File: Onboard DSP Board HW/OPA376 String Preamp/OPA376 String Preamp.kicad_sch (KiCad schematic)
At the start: 8 parts, among them U5 OPA376AIDCKT

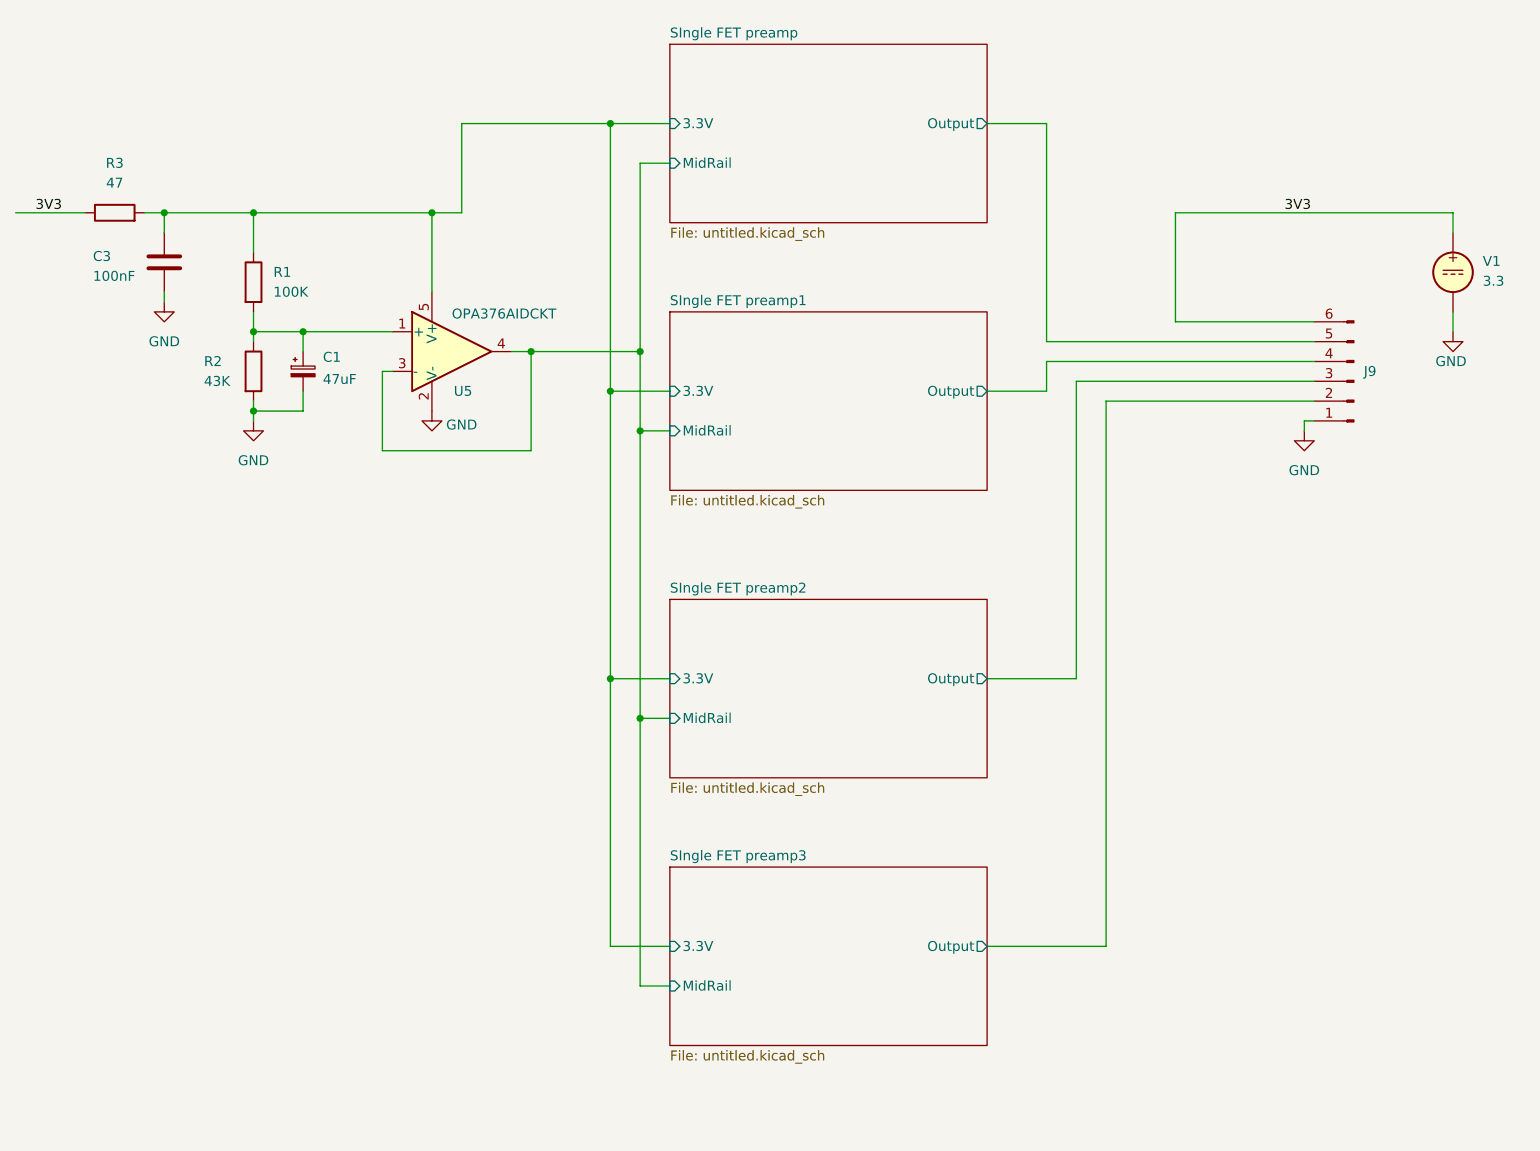
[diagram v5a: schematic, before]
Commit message: preamp board modified and simulated
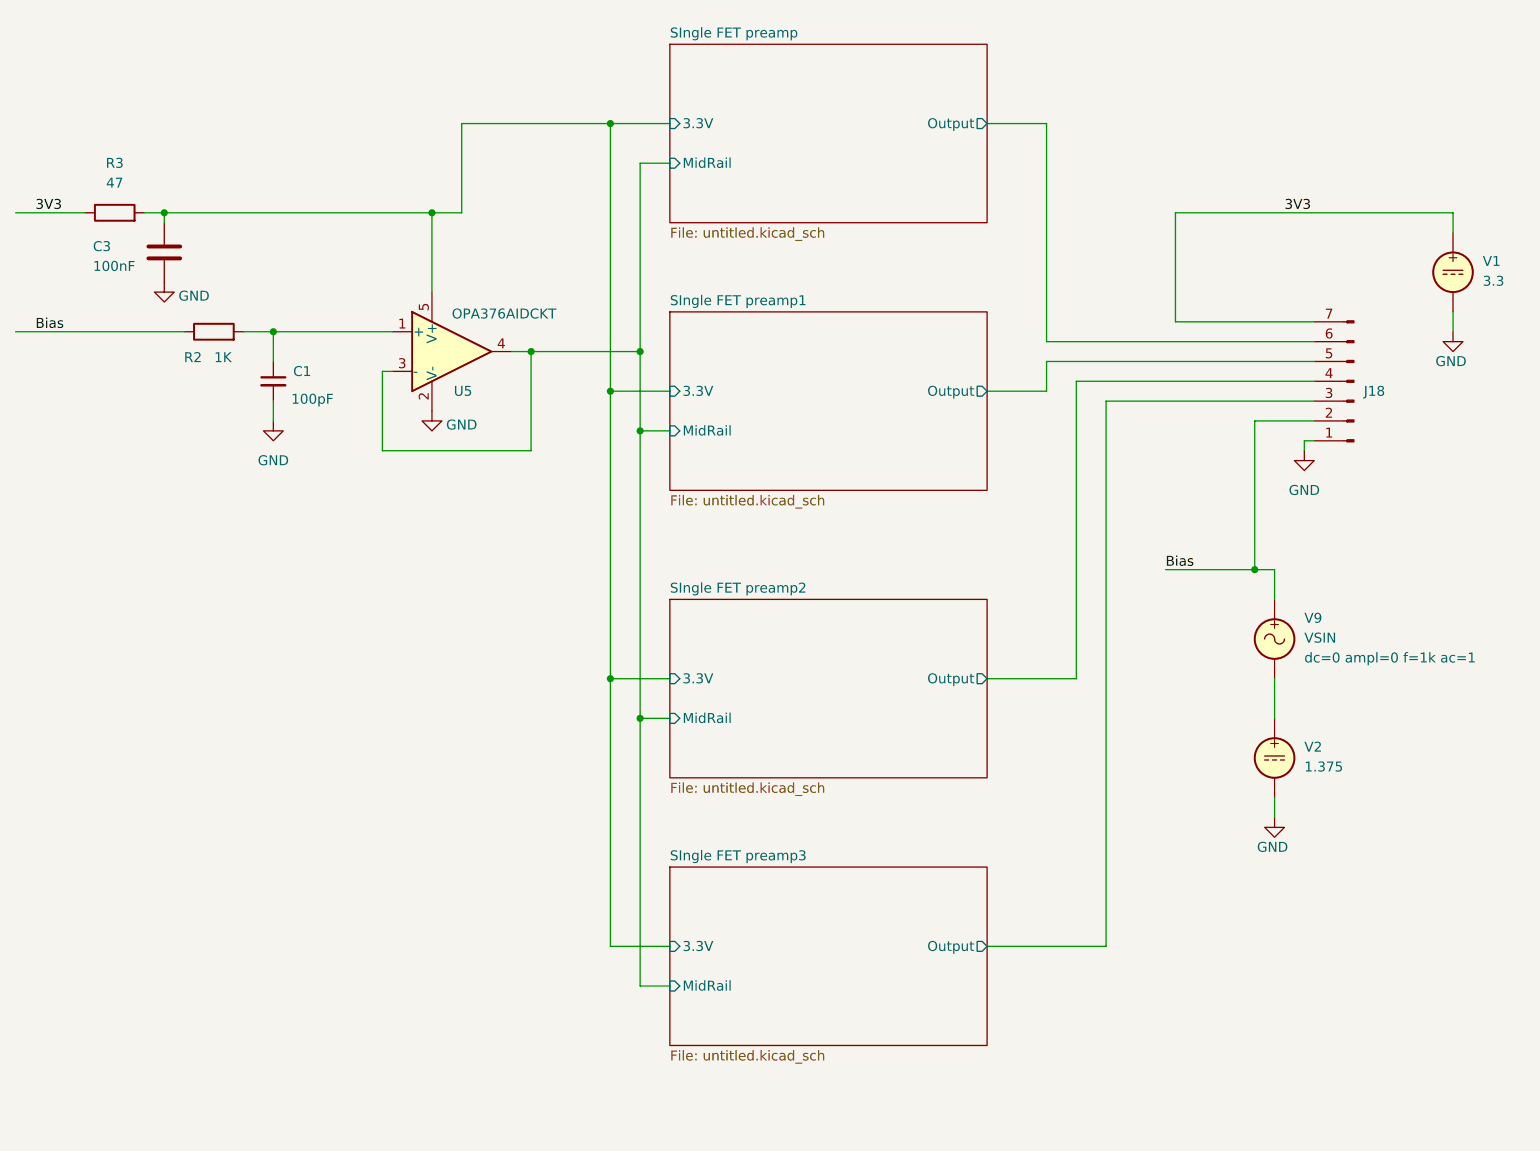
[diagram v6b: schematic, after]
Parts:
- removed C1: 47uF, Capacitor_Tantalum_SMD:CP_EIA-3216-12_Kemet-S, symbol Device:C_Polarized_Small
- removed J9: (no value), Connector_PinHeader_2.00mm:PinHeader_1x06_P2.00mm_Horizontal, symbol Connector:Conn_01x06_Pin
- removed R1: 100K, Resistor_SMD:R_0402_1005Metric, symbol Device:R
- added C1: 100pF, Capacitor_SMD:C_0402_1005Metric, symbol Device:C_Small
- added J18: (no value), Connector_PinHeader_2.00mm:PinHeader_1x07_P2.00mm_Horizontal, symbol Connector:Conn_01x07_Pin
- added V2: 1.375, symbol Simulation_SPICE:VDC
- added V9: VSIN, symbol Simulation_SPICE:VSIN
- R2: value 43K -> 1K
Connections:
- net 3V3: now also J18.7 (Pin_7)
- net GND: now also C1.2, J18.1 (Pin_1), V2.2; no longer R2.2
- net SIngle FET preamp/Output: now also J18.6 (Pin_6)
- net SIngle FET preamp1/Output: now also J18.5 (Pin_5)
- net SIngle FET preamp2/Output: now also J18.4 (Pin_4)
- net SIngle FET preamp3/Output: now also J18.3 (Pin_3)
- net at U5.1 (+): now also R2.2, C1.1; no longer R2.1
- new net: V2.1, V9.2
- new net Bias: J18.2 (Pin_2), R2.1, V9.1
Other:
- moved on the sheet: C3

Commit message: WIP
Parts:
- U5: value OPA376AIDCKT -> OPA376AIDCKR
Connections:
- net 3V3: now also J18.3 (Pin_3); no longer J18.7 (Pin_7)
- net SIngle FET preamp/Output: now also J18.7 (Pin_7); no longer J18.6 (Pin_6)
- net SIngle FET preamp1/Output: now also J18.6 (Pin_6); no longer J18.5 (Pin_5)
- net SIngle FET preamp2/Output: now also J18.5 (Pin_5); no longer J18.4 (Pin_4)
- net SIngle FET preamp3/Output: now also J18.4 (Pin_4); no longer J18.3 (Pin_3)
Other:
- moved on the sheet: J18
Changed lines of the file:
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@@
+	)
+	(junction
+		(at 199.39 101.6)
+		(diameter 0)
+		(color 0 0 0 0)
 	)
 	(junction
@@
 		(color 0 0 0 0)
 	)
-	(junction
-		(at 196.85 101.6)
-		(diameter 0)
-		(color 0 0 0 0)
-	)
 	(wire
 		(pts
@@
 	(wire
 		(pts
+			(xy 204.47 85.09) (xy 199.39 85.09)
+		)
+		(stroke
+			(width 0)
+			(type default)
+		)
+	)
+	(wire
+		(pts
 			(xy 121.92 49.53) (xy 118.11 49.53)
 		)
@@
 	(wire
 		(pts
-			(xy 186.69 69.85) (xy 204.47 69.85)
-		)
-		(stroke
-			(width 0)
-			(type default)
-		)
-	)
-	(wire
-		(pts
 			(xy 91.44 55.88) (xy 91.44 66.04)
 		)
@@
 	(wire
 		(pts
-			(xy 196.85 82.55) (xy 196.85 101.6)
-		)
-		(stroke
-			(width 0)
-			(type default)
-		)
-	)
-	(wire
-		(pts
 			(xy 170.18 74.93) (xy 204.47 74.93)
 		)
@@
 	(wire
 		(pts
-			(xy 222.25 55.88) (xy 186.69 55.88)
-		)
-		(stroke
-			(width 0)
-			(type default)
-		)
-	)
-	(wire
-		(pts
 			(xy 57.15 55.88) (xy 91.44 55.88)
 		)
@@
 	(wire
 		(pts
-			(xy 204.47 85.09) (xy 203.2 85.09)
+			(xy 204.47 87.63) (xy 203.2 87.63)
 		)
 		(stroke
@@
 	(wire
 		(pts
+			(xy 195.58 55.88) (xy 222.25 55.88)
+		)
+		(stroke
+			(width 0)
+			(type default)
+		)
+	)
+	(wire
+		(pts
 			(xy 118.11 49.53) (xy 118.11 73.66)
 		)
@@
 	(wire
 		(pts
-			(xy 204.47 82.55) (xy 196.85 82.55)
-		)
-		(stroke
-			(width 0)
-			(type default)
-		)
-	)
-	(wire
-		(pts
 			(xy 71.12 71.12) (xy 71.12 74.93)
 		)
@@
 	(wire
 		(pts
-			(xy 199.39 101.6) (xy 196.85 101.6)
-		)
-		(stroke
-			(width 0)
-			(type default)
-		)
-	)
-	(wire
-		(pts
 			(xy 162.56 78.74) (xy 170.18 78.74)
 		)
@@
 	(wire
 		(pts
-			(xy 186.69 55.88) (xy 186.69 69.85)
+			(xy 199.39 85.09) (xy 199.39 101.6)
+		)
+		(stroke
+			(width 0)
+			(type default)
+		)
+	)
+	(wire
+		(pts
+			(xy 195.58 55.88) (xy 195.58 82.55)
 		)
 		(stroke
@@
 	(wire
 		(pts
-			(xy 203.2 85.09) (xy 203.2 86.36)
+			(xy 203.2 87.63) (xy 203.2 88.9)
 		)
 		(stroke
@@
 	(wire
 		(pts
+			(xy 195.58 82.55) (xy 204.47 82.55)
+		)
+		(stroke
+			(width 0)
+			(type default)
+		)
+	)
+	(wire
+		(pts
 			(xy 204.47 77.47) (xy 173.99 77.47)
 		)
@@
 	(wire
 		(pts
-			(xy 185.42 101.6) (xy 196.85 101.6)
+			(xy 185.42 101.6) (xy 199.39 101.6)
 		)
 		(stroke
@@
 	)
 	(label "3V3"
-		(at 200.66 55.88 0)
+		(at 207.01 55.88 0)
 		(effects
 			(font
@@
 			)
 		)
-		(property "Value" "OPA376AIDCKT"
+		(property "Value" "OPA376AIDCKR"
 			(at 93.98 68.834 0)
 			(show_name no)
@@
 	(symbol
 		(lib_id "Connector:Conn_01x07_Pin")
-		(at 209.55 77.47 180)
+		(at 209.55 80.01 180)
 		(unit 1)
 		(body_style 1)
@@
 		(dnp no)
 		(property "Reference" "J18"
+			(at 210.82 81.2801 0)
+			(show_name no)
+			(do_not_autoplace no)
+			(effects
+				(font
+					(size 1.27 1.27)
+				)
+				(justify right)
+			)
+		)
+		(property "Value" ""
 			(at 210.82 78.7401 0)
 			(show_name no)
@@
 			)
 		)
-		(property "Value" ""
-			(at 210.82 76.2001 0)
-			(show_name no)
-			(do_not_autoplace no)
-			(effects
-				(font
-					(size 1.27 1.27)
-				)
-				(justify right)
-			)
-		)
 		(property "Footprint" "Connector_PinHeader_2.00mm:PinHeader_1x07_P2.00mm_Horizontal"
-			(at 209.55 77.47 0)
+			(at 209.55 80.01 0)
 			(hide yes)
 			(show_name no)
@@
 		)
 		(property "Datasheet" ""
-			(at 209.55 77.47 0)
+			(at 209.55 80.01 0)
 			(hide yes)
 			(show_name no)
@@
 		)
 		(property "Description" "Generic connector, single row, 01x07, script generated"
-			(at 209.55 77.47 0)
+			(at 209.55 80.01 0)
 			(hide yes)
 			(show_name no)
@@
 	(symbol
 		(lib_id "power:GND")
-		(at 203.2 86.36 0)
+		(at 203.2 88.9 0)
 		(unit 1)
 		(body_style 1)
@@
 		(fields_autoplaced yes)
 		(property "Reference" "#PWR02"
-			(at 203.2 92.71 0)
+			(at 203.2 95.25 0)
 			(hide yes)
 			(show_name no)
@@
 		)
 		(property "Value" "GND"
-			(at 203.2 91.44 0)
+			(at 203.2 93.98 0)
 			(show_name no)
 			(do_not_autoplace no)
@@
 		)
 		(property "Footprint" ""
-			(at 203.2 86.36 0)
+			(at 203.2 88.9 0)
 			(hide yes)
 			(show_name no)
@@
 		)
 		(property "Datasheet" ""
-			(at 203.2 86.36 0)
+			(at 203.2 88.9 0)
 			(hide yes)
 			(show_name no)
@@
 		)
 		(property "Description" "Power symbol creates a global label with name \"GND\" , ground"
-			(at 203.2 86.36 0)
-			(hide yes)
-			(show_name no)
+			(at 203.2 88.9 0)
+			(hide yes)
+			(show_name no)
